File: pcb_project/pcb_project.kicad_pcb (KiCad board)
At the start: 6 copper layers, 246 parts, among them IC1 TPS54325PWPR, IC2 TPS54294PWPR, IC3 IS61WV204816BLL-10TLI, IC4 IS61WV204816BLL-10TLI, J10 M20-9990246, J11 M20-9990246, J12 M20-9990246, J13 Conn_01x10_Pin, J2 FTSH-107-01-F-DV-K, J3 Conn_ST_STDC14, J4 DE15_Socket_HighDensity_Mount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, J5 USB_B_Micro, J6 MEM2052-00-195-00-A, J7 USB_A, J8 M20-9990246, J9 M20-9990246, Q1 BC857BS, Q2 BC847BPN, SW2 SW_SPDT, SW3 SW_SPST, SW4 SW_SPST, U1 XC7A100T-FTG256, U10 TPD1E1B04DPYT, U11 TPD1E1B04DPYT, U12 TPD1E1B04DPYT, U13 TPD1E1B04DPYT, U2 STM32U595VJTx, U3 TPS2041B, U4 D3V3XA4B10LP, U5 TPD1E1B04DPYT, U6 TPD1E1B04DPYT, U7 MAX7221xWG, U8 COM-11405, U9 MT25QL128ABA1ESE-0SIT, Y1 48MHz, Y2 XLH736025.175000I

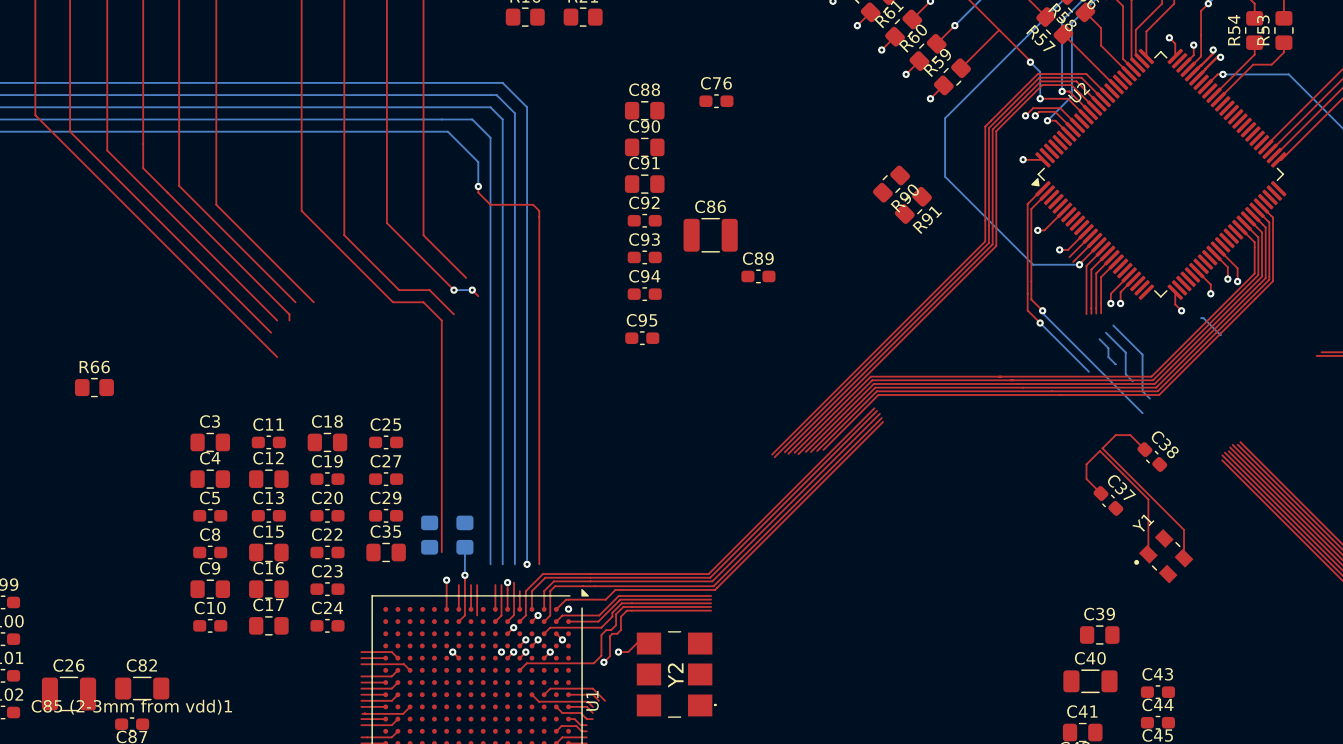
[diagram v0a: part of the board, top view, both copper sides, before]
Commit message: Change FPGA OSPI pins and connect to MCU only top layer
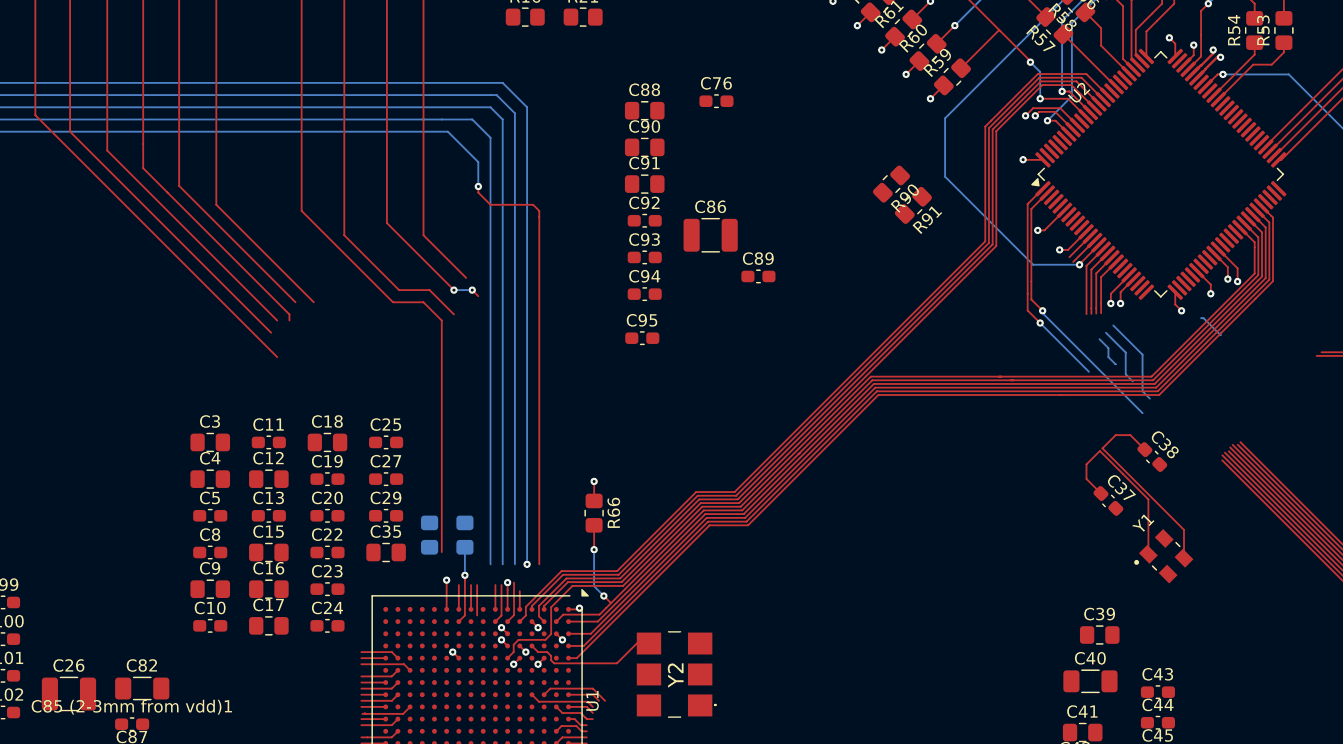
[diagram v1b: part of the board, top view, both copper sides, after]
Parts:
- moved R66 42.3 mm to (96.0, 97.8), turned to -90 degrees
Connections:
- U1 pad A2: /FPGA/OSPI 3 -> /FPGA/OSPI 0
- U1 pad A3: unconnected-(U1B-IO_L4N_T0_35-PadA3) -> /FPGA/OSPI 1
- U1 pad A4: unconnected-(U1B-IO_L3N_T0_DQS_AD5N_35-PadA4) -> /FPGA/OSPI 2
- U1 pad A5: unconnected-(U1B-IO_L3P_T0_DQS_AD5P_35-PadA5) -> /FPGA/OSPI 3
- U1 pad B1: /FPGA/OSPI 0 -> unconnected-(U1B-IO_L9N_T1_DQS_AD7N_35-PadB1)
- U1 pad B2: /FPGA/OSPI 4 -> /FPGA/OSPI CS
- U1 pad C1: /FPGA/OSPI 1 -> /FPGA/OSPI 7
- U1 pad C2: /FPGA/OSPI 5 -> /FPGA/OSPI 6
- U1 pad C3: /FPGA/OSPI 7 -> unconnected-(U1B-IO_L7P_T1_AD6P_35-PadC3)
- U1 pad D1: /FPGA/OSPI 2 -> /FPGA/OSPI 5
- U1 pad E2: /FPGA/OSPI 6 -> /FPGA/OSPI 4
- U1 pad E6: /FPGA/OSPI CS -> unconnected-(U1B-IO_0_35-PadE6)
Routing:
- net /FPGA/OSPI 3: track 61.8 -> 77.4 mm
- net /FPGA/OSPI CS: track 68.1 -> 81.4 mm, vias 0 -> 2
- net /FPGA/OSPI 4: track 60.3 -> 73.5 mm
- net /FPGA/OSPI CLK: track 68.9 -> 80.5 mm, vias 2 -> 0
- net /FPGA/OSPI 6: track 82.2 -> 71.5 mm
- net /FPGA/OSPI 7: track 58.9 -> 69.5 mm
- net /FPGA/OSPI 5: track 81.9 -> 71.4 mm
- net /FPGA/OSPI 1: track 84.0 -> 74.9 mm
- net /FPGA/OSPI 2: track 85.0 -> 76.1 mm
- net /FPGA/OSPI 0: track 81.8 -> 73.8 mm
- net +3V3: track 75.5 -> 77.1 mm, vias 24 -> 25
- net GND: track 4.61 -> 5.52 mm
- net /VGA/R1: track 98.2 -> 98.9 mm, vias 1 -> 2
- net Net-(U1B-IO_L12P_T1_MRCC_35): track 10.6 -> 11.2 mm, vias 2 -> 0
- net (no net): vias 14 -> 13

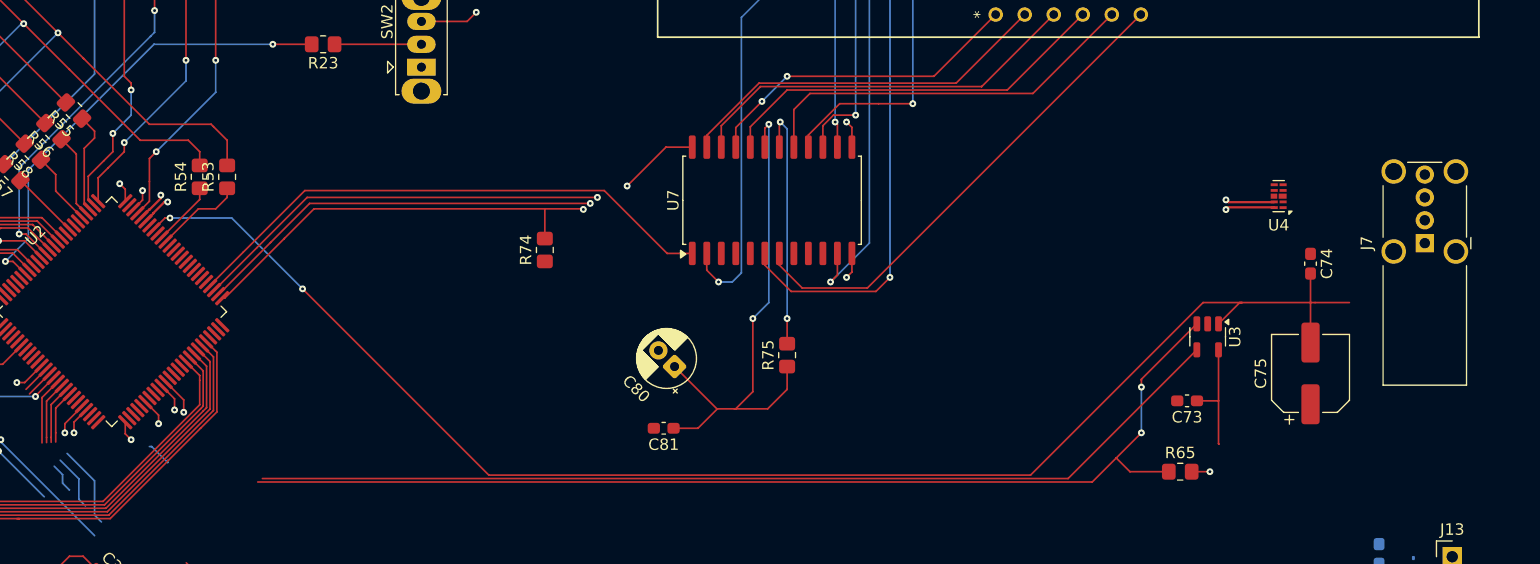
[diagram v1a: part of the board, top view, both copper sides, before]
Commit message: Layout with proper USB component
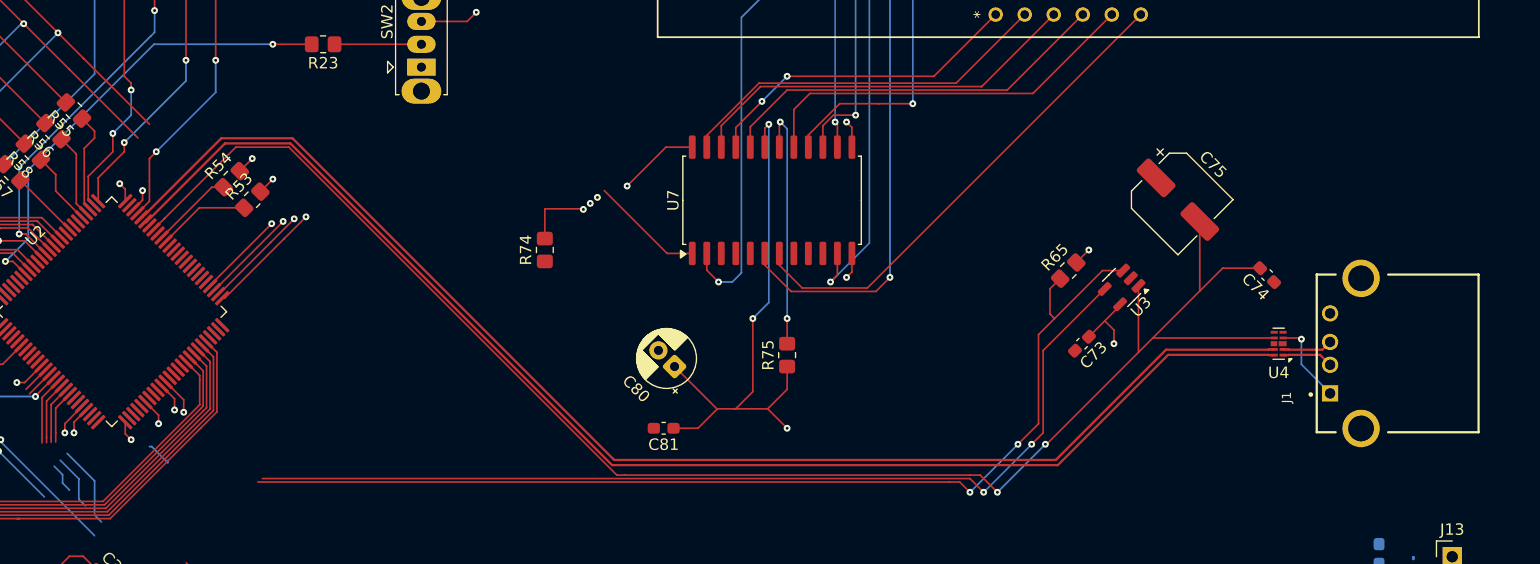
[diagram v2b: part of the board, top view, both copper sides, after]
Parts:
- removed J7: USB_A, Connector_USB:USB_A_Wuerth_614004134726_Horizontal
- added J1: USB1130-15-A_REVA, Project_Footprints:GCT_USB1130-15-A_REVA, F.Cu at (251.8, 73.6)
- moved R65 20.1 mm to (226.2, 66.4), turned to 45 degrees
- moved C75 19.1 mm to (235.8, 60.2), turned to -45 degrees
- moved U4 12.9 mm to (244.6, 72.8)
- moved C73 10.5 mm to (227.4, 72.8), turned to -135 degrees
- moved U3 8.69 mm to (230.9, 67.9), turned to -135 degrees
- moved C74 3.93 mm to (243.6, 66.8), turned to 135 degrees
- moved R53 2.97 mm to (154.8, 60.2), turned to 45 degrees
- moved R54 2.81 mm to (153.0, 58.4), turned to 45 degrees
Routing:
- net /7_segment_led+IC/LED_MOSI: track 48.0 -> 17.7 mm, vias 0 -> 1
- net /7_segment_led+IC/LED_MISO: track 47.0 -> 18.6 mm, vias 2 -> 3
- net /7_segment_led+IC/LED_CLK: track 63.6 -> 37.2 mm, vias 2 -> 3
- net /MCU/PA9_OTG_HS_VBUS: track 129.5 -> 151.1 mm, vias 2 -> 3
- net /7_segment_led+IC/LED_CS: track 65.3 -> 44.1 mm, vias 2 -> 3
- net Net-(J6-DAT0): track 72.1 -> 64.1 mm, vias 4 -> 5
- net Net-(J6-DAT1): track 65.8 -> 60.3 mm, vias 4 -> 5
- net /MCU/OTG_HS_D-: track 117.4 -> 121.8 mm, vias 2 -> 0
- net /MCU/OTG_HS_D+: track 117.9 -> 122.1 mm, vias 2 -> 0
- net /MCU/PB0_LPGPIO1_P9: track 98.3 -> 95.3 mm
- net /MCU/PC9_SDMMC1_D1: track 5.69 -> 7.25 mm
- net +5V: track 57.1 -> 55.7 mm, vias 2 -> 4
- net /MCU/PB1_LPGPIO1_P3: track 89.7 -> 89.1 mm, vias 1 -> 3

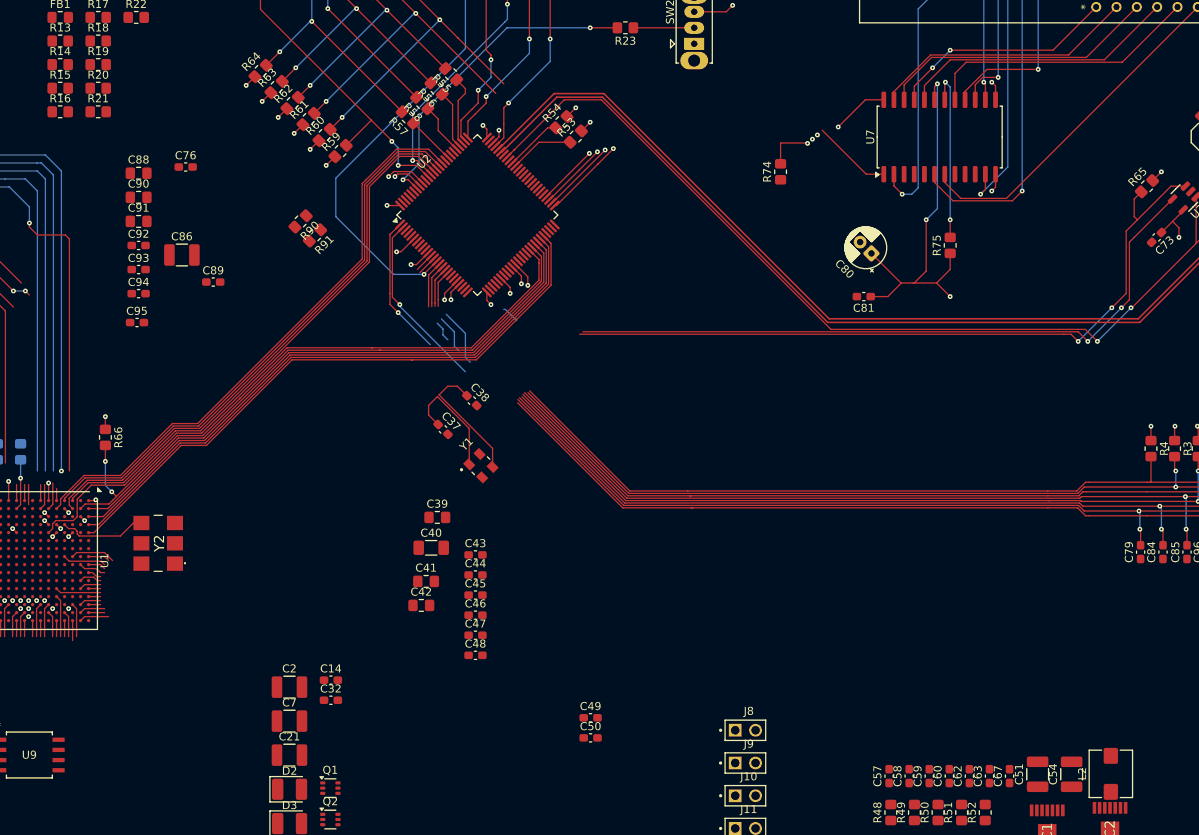
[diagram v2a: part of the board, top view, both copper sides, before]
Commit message: Clean up routing around MCU and ish length match OSPI
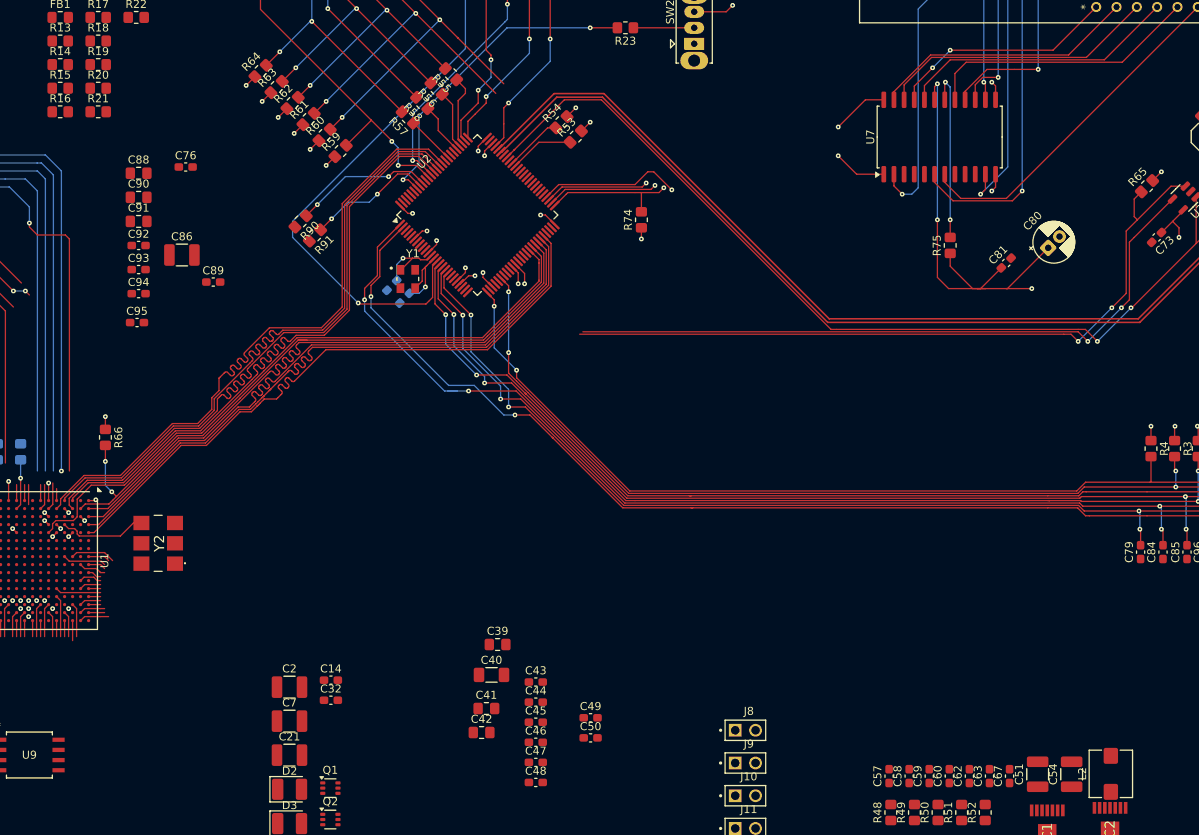
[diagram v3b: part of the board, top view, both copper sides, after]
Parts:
- C37, C38: moved to B.Cu
- moved Y1 25.1 mm to (133.8, 78.0), turned to 0 degrees
- moved C80 22.1 mm to (213.8, 74.1), turned to 45 degrees
- moved C37 19.1 mm to (131.8, 78.8), turned to -135 degrees
- moved R74 18.4 mm to (163.0, 70.6)
- moved C81 18.3 mm to (208.6, 76.0), turned to 45 degrees
- moved C43 17.6 mm to (149.8, 128.4)
- moved C45 17.6 mm to (149.8, 133.4)
- moved C46 17.6 mm to (149.8, 135.9)
- moved C48 17.6 mm to (149.8, 140.9)
- moved C39 17.6 mm to (145.0, 123.7)
- moved C40 17.6 mm to (144.3, 127.5)
- moved C41 17.6 mm to (143.6, 131.7)
- moved C42 17.6 mm to (143.0, 134.7)
- moved C44 17.6 mm to (149.8, 130.9)
- moved C47 17.6 mm to (149.8, 138.4)
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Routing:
- net /7_segment_led+IC/LED_MOSI: track 17.7 -> 48.0 mm, vias 1 -> 2
- net /7_segment_led+IC/LED_MISO: track 18.6 -> 47.0 mm, vias 3 -> 2
- net /7_segment_led+IC/LED_CLK: track 37.2 -> 63.7 mm, vias 3 -> 2
- net /7_segment_led+IC/LED_CS: track 44.1 -> 65.0 mm, vias 3 -> 2
- net /MCU/PE2_LPGPIO1_P14: track 130.0 -> 150.3 mm, vias 3 -> 4
- net /MCU/PC0_ADC1_IN1: track 115.2 -> 132.7 mm, vias 2 -> 4
- net Net-(D11-K): track 111.2 -> 125.7 mm
- net /MCU/PC1_ADC1_IN2: track 116.0 -> 130.4 mm, vias 2 -> 4
- net /MCU/PA6_LPGPIO1_P2: track 113.8 -> 127.2 mm, vias 3 -> 4
- net /MCU/PE3_LPGPIO1_P15: track 140.0 -> 152.7 mm, vias 3 -> 4
- net Net-(U2-PB6): track 5.10 -> 17.4 mm, vias 1 -> 2
- net Net-(U2-PB7): track 3.85 -> 15.9 mm, vias 1 -> 2
- net /MCU/PC2_ADC1_IN3: track 118.2 -> 129.9 mm, vias 2 -> 4
- net /MCU/PA3_LPGPIO1_P1: track 115.7 -> 126.1 mm, vias 1 -> 2
- net /FPGA/OSPI 7: track 69.5 -> 79.3 mm
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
